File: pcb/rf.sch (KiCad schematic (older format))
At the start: 28 parts, among them U3 STM32W108C8, U4 SE2432L

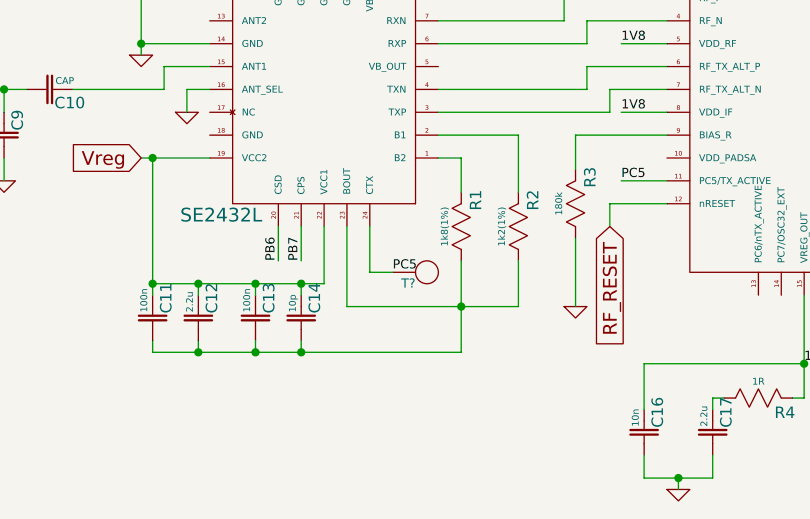
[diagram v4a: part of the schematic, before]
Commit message: Added MCP6409 and audio preamp schematic
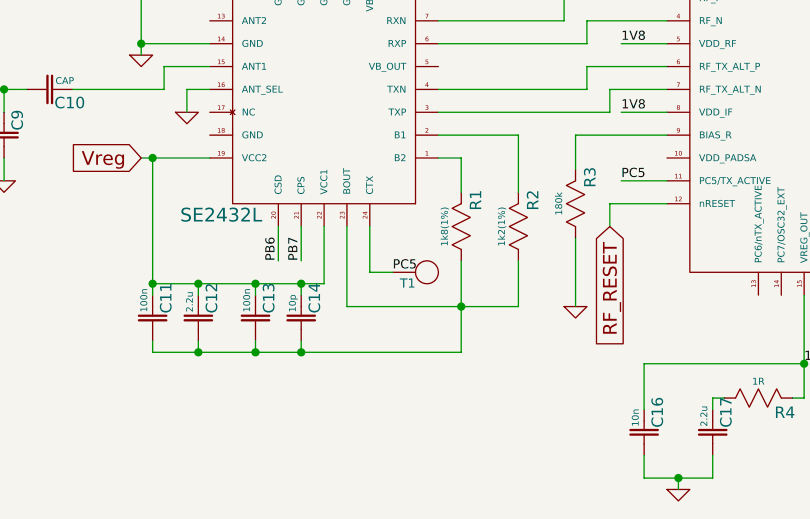
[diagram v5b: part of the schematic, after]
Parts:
- gave numbers to parts that had none: 1
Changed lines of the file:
@@
-EESchema Schematic File Version 2  date 7/25/2012 8:49:54 PM
+EESchema Schematic File Version 2  date Thu 26 Jul 2012 01:52:34 AM EDT
 LIBS:power
 LIBS:device
@@
 LIBS:valves
 LIBS:f4_daughter
+LIBS:f4_daughter-cache
 EELAYER 25  0
 EELAYER END
-$Descr A4 11700 8267
+$Descr A4 11693 8268
 encoding utf-8
-Sheet 2 4
+Sheet 2 5
 Title ""
 Date "26 jul 2012"
@@
 PC5
 $Comp
-L GND #PWR01
+L GND #PWR13
 U 1 1 500DD937
 P 8250 4650
-F 0 "#PWR01" H 8250 4650 30  0001 C CNN
+F 0 "#PWR13" H 8250 4650 30  0001 C CNN
 F 1 "GND" H 8250 4580 30  0001 C CNN
 	1    8250 4650
@@
 $EndComp
 $Comp
-L GND #PWR02
+L GND #PWR5
 U 1 1 500DD8E1
 P 3850 4200
-F 0 "#PWR02" H 3850 4200 30  0001 C CNN
+F 0 "#PWR5" H 3850 4200 30  0001 C CNN
 F 1 "GND" H 3850 4130 30  0001 C CNN
 	1    3850 4200
@@
 $EndComp
 $Comp
-L GND #PWR03
+L GND #PWR12
 U 1 1 500DD883
 P 8100 3050
-F 0 "#PWR03" H 8100 3050 30  0001 C CNN
+F 0 "#PWR12" H 8100 3050 30  0001 C CNN
 F 1 "GND" H 8100 2980 30  0001 C CNN
 	1    8100 3050
@@
 1V2
 $Comp
-L GND #PWR04
+L GND #PWR8
 U 1 1 500DD7C0
 P 5800 3200
-F 0 "#PWR04" H 5800 3200 30  0001 C CNN
+F 0 "#PWR8" H 5800 3200 30  0001 C CNN
 F 1 "GND" H 5800 3130 30  0001 C CNN
 	1    5800 3200
@@
 $EndComp
 $Comp
-L GND #PWR05
+L GND #PWR10
 U 1 1 500DD6F0
 P 7550 5650
-F 0 "#PWR05" H 7550 5650 30  0001 C CNN
+F 0 "#PWR10" H 7550 5650 30  0001 C CNN
 F 1 "GND" H 7550 5580 30  0001 C CNN
 	1    7550 5650
@@
 Vreg
 $Comp
-L GND #PWR06
+L GND #PWR6
 U 1 1 500DD2FF
 P 5000 3650
-F 0 "#PWR06" H 5000 3650 30  0001 C CNN
+F 0 "#PWR6" H 5000 3650 30  0001 C CNN
 F 1 "GND" H 5000 3580 30  0001 C CNN
 	1    5000 3650
@@
 $EndComp
 $Comp
-L GND #PWR07
+L GND #PWR9
 U 1 1 500DD1EA
 P 6000 5850
-F 0 "#PWR07" H 6000 5850 30  0001 C CNN
+F 0 "#PWR9" H 6000 5850 30  0001 C CNN
 F 1 "GND" H 6000 5780 30  0001 C CNN
 	1    6000 5850
@@
 $EndComp
 $Comp
-L GND #PWR08
+L GND #PWR7
 U 1 1 500DCCCC
 P 5550 5050
-F 0 "#PWR08" H 5550 5050 30  0001 C CNN
+F 0 "#PWR7" H 5550 5050 30  0001 C CNN
 F 1 "GND" H 5550 4980 30  0001 C CNN
 	1    5550 5050
@@
 1V8
 $Comp
-L GND #PWR09
+L GND #PWR3
 U 1 1 500DCAB4
 P 3050 4500
-F 0 "#PWR09" H 3050 4500 30  0001 C CNN
+F 0 "#PWR3" H 3050 4500 30  0001 C CNN
 F 1 "GND" H 3050 4430 30  0001 C CNN
 	1    3050 4500
@@
 $EndComp
 $Comp
-L GND #PWR010
+L GND #PWR2
 U 1 1 500DCAB1
 P 2200 4500
-F 0 "#PWR010" H 2200 4500 30  0001 C CNN
+F 0 "#PWR2" H 2200 4500 30  0001 C CNN
 F 1 "GND" H 2200 4430 30  0001 C CNN
 	1    2200 4500
@@
 $EndComp
 $Comp
-L GND #PWR011
+L GND #PWR4
 U 1 1 500DCAA7
 P 3650 3950
-F 0 "#PWR011" H 3650 3950 30  0001 C CNN
+F 0 "#PWR4" H 3650 3950 30  0001 C CNN
 F 1 "GND" H 3650 3880 30  0001 C CNN
 	1    3650 3950
@@
 $EndComp
 $Comp
-L GND #PWR012
+L GND #PWR1
 U 1 1 500DCA40
 P 1800 4200
-F 0 "#PWR012" H 1800 4200 30  0001 C CNN
+F 0 "#PWR1" H 1800 4200 30  0001 C CNN
 F 1 "GND" H 1800 4130 30  0001 C CNN
 	1    1800 4200
@@
 $EndComp
 $Comp
-L GND #PWR013
+L GND #PWR11
 U 1 1 500DCA3C
 P 8050 4950
-F 0 "#PWR013" H 8050 4950 30  0001 C CNN
+F 0 "#PWR11" H 8050 4950 30  0001 C CNN
 F 1 "GND" H 8050 4880 30  0001 C CNN
 	1    8050 4950
@@
 $EndComp
 $Comp
-L TP T?
+L TP T1
 U 1 1 500EC307
 P 4850 4900
-F 0 "T?" H 4850 4875 40  0000 R TNN
+F 0 "T1" H 4850 4875 40  0000 R TNN
 F 1 "TP" H 4800 4950 60  0001 C CNN
 	1    4850 4900

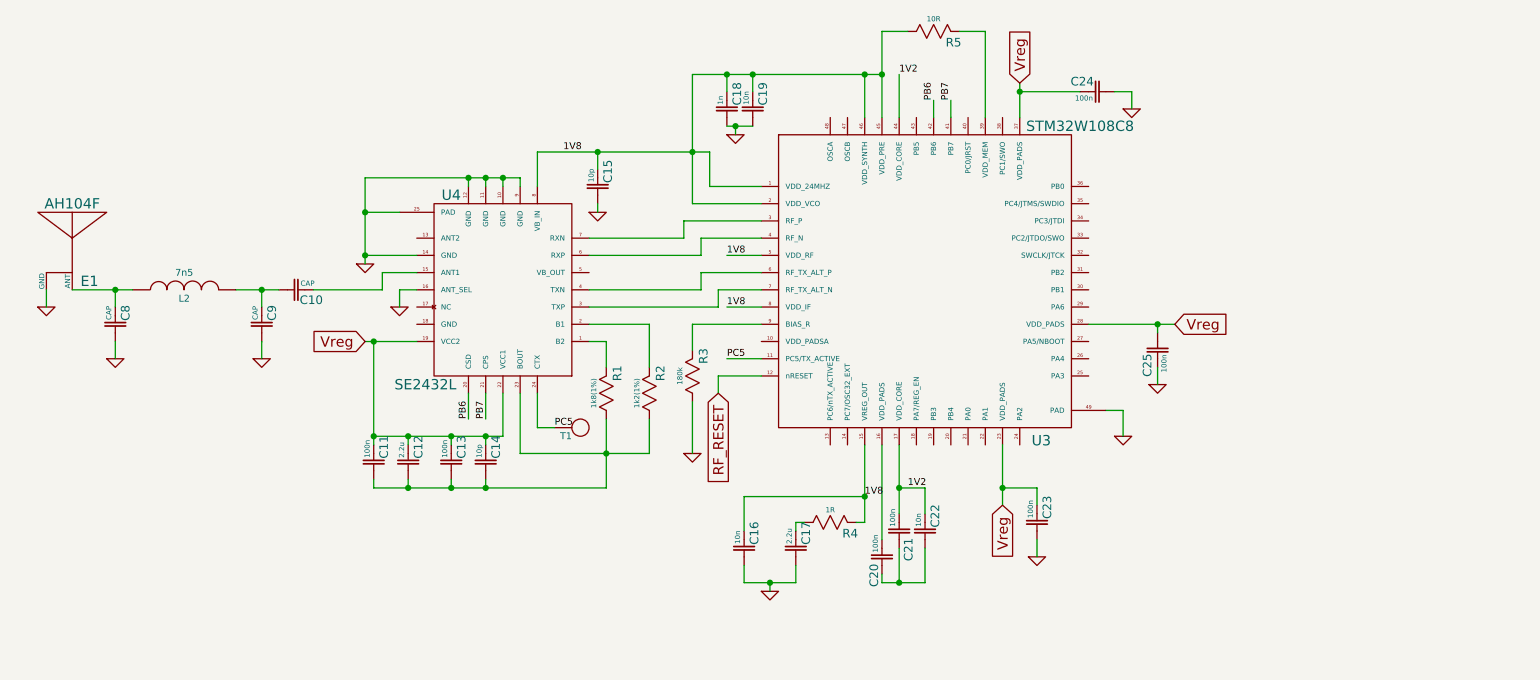
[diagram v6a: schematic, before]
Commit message: Added LCD and started wiring busses
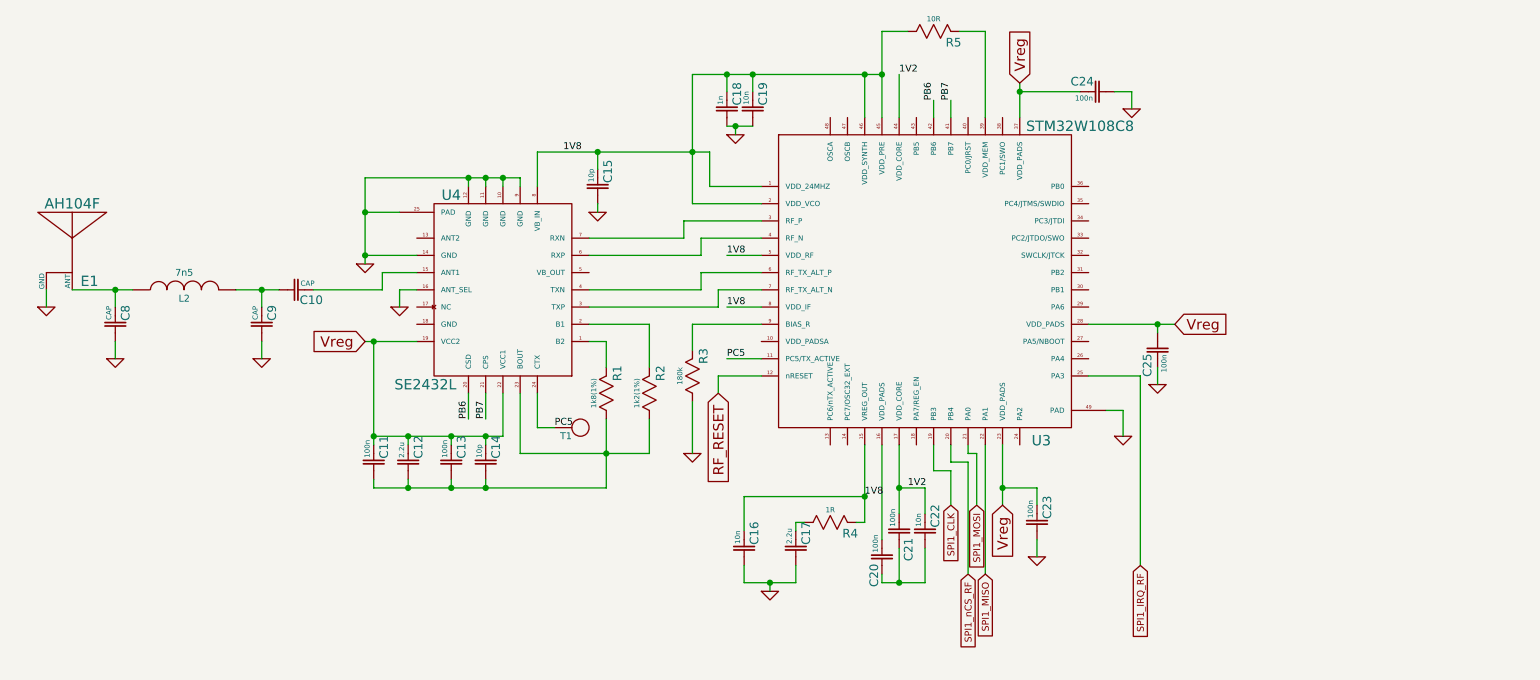
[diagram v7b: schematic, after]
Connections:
- net SPI1_CLK: now reaches U3.19 (PB3)
- net SPI1_nCS_RF: now reaches U3.20 (PB4)
- net SPI1_MOSI: now reaches U3.21 (PA0)
- net SPI1_MISO: now reaches U3.22 (PA1)
- net SPI1_IRQ_RF: now reaches U3.25 (PA3)
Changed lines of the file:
@@
-EESchema Schematic File Version 2  date Thu 26 Jul 2012 02:06:26 AM EDT
+EESchema Schematic File Version 2  date Thu 26 Jul 2012 11:54:13 PM EDT
 LIBS:power
 LIBS:device
@@
 Sheet 2 5
 Title ""
-Date "26 jul 2012"
+Date "27 jul 2012"
 Rev ""
 Comp ""
@@
 Connection ~ 6650 2850
 Wire Wire Line
-	6650 3100 6650 2600
+	6650 2600 6650 3100
 Wire Wire Line
 	6650 2600 6800 2600
@@
 Connection ~ 5550 3300
 Wire Wire Line
-	5650 3300 4650 3300
+	4650 3300 5650 3300
 Wire Wire Line
 	5650 3300 5650 3500
@@
 Connection ~ 3700 4950
 Wire Wire Line
-	3700 5000 3700 4400
+	3700 4400 3700 5000
 Wire Wire Line
 	3650 4400 3950 4400
@@
 Connection ~ 5050 5050
 Wire Wire Line
-	5300 5050 4550 5050
+	4550 5050 5300 5050
 Wire Wire Line
 	4950 4300 5300 4300
@@
 	3650 3450 4550 3450
 Wire Wire Line
-	3650 3950 3650 3450
+	3650 3450 3650 3950
 Connection ~ 3650 3650
 Connection ~ 4250 3450
@@
 	6150 5800 6150 5700
 Wire Wire Line
-	6150 5800 5850 5800
+	5850 5800 6150 5800
 Wire Wire Line
 	5850 5800 5850 5700
@@
 	5550 2850 5550 3600
 Wire Wire Line
-	6650 2850 5550 2850
+	5550 2850 6650 2850
 Wire Wire Line
 	6750 3100 6750 2850
@@
 	1    0    0    -1
 $EndComp
+Text GLabel 7050 5350 3    40   Input ~ 0
+SPI1_CLK
+Wire Wire Line
+	7050 5350 7050 5150
+Wire Wire Line
+	7050 5150 6950 5150
+Wire Wire Line
+	6950 5150 6950 5000
+Text GLabel 7150 5750 3    40   Input ~ 0
+SPI1_nCS_RF
+Wire Wire Line
+	7150 5750 7150 5100
+Wire Wire Line
+	7150 5100 7050 5100
+Wire Wire Line
+	7050 5100 7050 5000
+Text GLabel 7200 5350 3    40   Input ~ 0
+SPI1_MOSI
+Wire Wire Line
+	7200 5350 7200 5050
+Wire Wire Line
+	7200 5050 7150 5050
+Wire Wire Line
+	7150 5050 7150 5000
+Text GLabel 7250 5750 3    40   Input ~ 0
+SPI1_MISO
+Wire Wire Line
+	7250 5750 7250 5000
+Text GLabel 8150 5700 3    40   Input ~ 0
+SPI1_IRQ_RF
+Wire Wire Line
+	8150 5700 8150 4600
+Wire Wire Line
+	8150 4600 7850 4600
 $EndSCHEMATC

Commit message: Broke up schematic in a more modular fashion -- Added LCD footprint
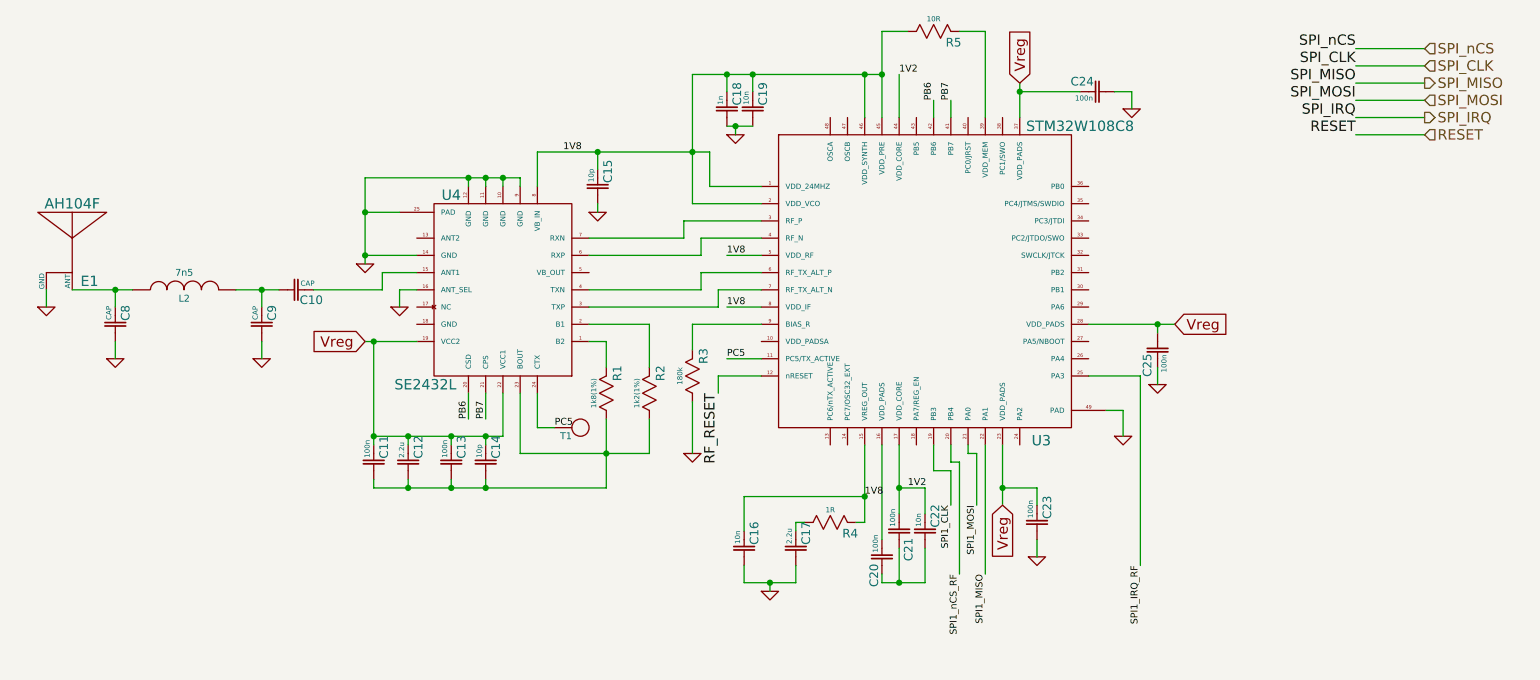
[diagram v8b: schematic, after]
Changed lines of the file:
@@
-EESchema Schematic File Version 2  date Thu 26 Jul 2012 11:54:13 PM EDT
+EESchema Schematic File Version 2  date Tue 31 Jul 2012 10:29:35 PM EDT
 LIBS:power
 LIBS:device
@@
 EELAYER 25  0
 EELAYER END
-$Descr A4 11693 8268
+$Descr A4 11700 8267
 encoding utf-8
-Sheet 2 5
+Sheet 4 6
 Title ""
-Date "27 jul 2012"
+Date "1 aug 2012"
 Rev ""
 Comp ""
@@
 $EndDescr
 Wire Wire Line
+	9800 2700 9400 2700
+Wire Wire Line
+	9800 2900 9400 2900
+Wire Wire Line
+	9800 3100 9400 3100
+Wire Wire Line
 	7050 3000 7050 3100
 Wire Wire Line
@@
 Connection ~ 8250 4300
 Wire Wire Line
-	7850 4300 8350 4300
+	8350 4300 7850 4300
 Connection ~ 6650 2850
 Wire Wire Line
-	6650 2600 6650 3100
+	6650 3100 6650 2600
 Wire Wire Line
 	6650 2600 6800 2600
@@
 Connection ~ 5800 3150
 Wire Wire Line
-	5750 3150 5900 3150
+	5900 3150 5750 3150
 Connection ~ 5550 3300
 Wire Wire Line
-	4650 3300 5650 3300
+	5650 3300 4650 3300
 Wire Wire Line
 	5650 3300 5650 3500
@@
 	5650 3500 5950 3500
 Wire Wire Line
-	6650 5800 6650 5750
+	6650 5750 6650 5800
 Wire Wire Line
 	6750 5600 6750 5800
@@
 Connection ~ 6750 5250
 Wire Wire Line
-	6900 5250 6750 5250
+	6750 5250 6900 5250
 Wire Wire Line
 	6900 5250 6900 5400
 Connection ~ 7350 5250
 Wire Wire Line
-	7550 5250 7350 5250
+	7350 5250 7550 5250
 Wire Wire Line
 	7550 5250 7550 5350
@@
 	3900 5250 3900 5200
 Wire Wire Line
-	3700 5250 3700 5200
+	3700 5200 3700 5250
 Connection ~ 4150 4950
 Wire Wire Line
@@
 Connection ~ 3700 4950
 Wire Wire Line
-	3700 4400 3700 5000
-Wire Wire Line
-	3650 4400 3950 4400
+	3700 5000 3700 4400
+Wire Wire Line
+	3950 4400 3650 4400
 Connection ~ 6550 5300
 Wire Wire Line
-	5850 5300 6550 5300
+	6550 5300 5850 5300
 Wire Wire Line
 	5850 5300 5850 5500
@@
 	5000 3650 5000 3600
 Wire Wire Line
-	6550 5450 6500 5450
-Wire Wire Line
-	6550 5000 6550 5450
-Wire Wire Line
-	5300 5050 5300 4850
+	6500 5450 6550 5450
+Wire Wire Line
+	6550 5450 6550 5000
+Wire Wire Line
+	5300 4850 5300 5050
 Wire Wire Line
 	5050 4550 5050 4400
 Connection ~ 5050 5050
 Wire Wire Line
-	4550 5050 5300 5050
+	5300 5050 4550 5050
 Wire Wire Line
 	4950 4300 5300 4300
@@
 Connection ~ 4450 3450
 Wire Wire Line
-	4550 3450 4550 3500
+	4550 3500 4550 3450
 Wire Wire Line
 	4350 3450 4350 3500
@@
 Connection ~ 2200 4100
 Wire Wire Line
-	1950 4100 2300 4100
+	2300 4100 1950 4100
 Wire Wire Line
 	1800 4200 1800 4100
 Wire Wire Line
-	2900 4100 3150 4100
+	3150 4100 2900 4100
 Connection ~ 3050 4100
 Wire Wire Line
@@
 Connection ~ 4350 3450
 Wire Wire Line
-	3650 3450 4550 3450
+	4550 3450 3650 3450
 Wire Wire Line
 	3650 3450 3650 3950
@@
 	3750 4100 3350 4100
 Wire Wire Line
-	6150 5800 6150 5700
-Wire Wire Line
-	5850 5800 6150 5800
+	6150 5700 6150 5800
+Wire Wire Line
+	6150 5800 5850 5800
 Wire Wire Line
 	5850 5800 5850 5700
@@
 Connection ~ 3900 5250
 Wire Wire Line
-	5050 5250 3700 5250
-Wire Wire Line
-	5050 4850 5050 5250
+	3700 5250 5050 5250
+Wire Wire Line
+	5050 5250 5050 4850
 Connection ~ 4350 5250
 Wire Wire Line
-	7350 5000 7350 5350
+	7350 5350 7350 5000
 Wire Wire Line
 	7550 5650 7550 5550
 Wire Wire Line
-	6750 5000 6750 5400
+	6750 5400 6750 5000
 Wire Wire Line
 	6650 5800 6900 5800
@@
 	6900 5800 6900 5600
 Wire Wire Line
-	5550 3600 5950 3600
+	5950 3600 5550 3600
 Connection ~ 5000 3300
 Wire Wire Line
 	5800 3200 5800 3150
 Wire Wire Line
-	5550 2850 5550 3600
+	5550 3600 5550 2850
 Wire Wire Line
 	5550 2850 6650 2850
@@
 	8100 2950 8000 2950
 Wire Wire Line
-	7450 2900 7450 3100
+	7450 3100 7450 2900
 Connection ~ 7450 2950
 Wire Wire Line
@@
 Wire Wire Line
 	6950 3000 6950 3100
+Wire Wire Line
+	7050 5350 7050 5150
+Wire Wire Line
+	7050 5150 6950 5150
+Wire Wire Line
+	6950 5150 6950 5000
+Wire Wire Line
+	7100 5750 7100 5100
+Wire Wire Line
+	7100 5100 7050 5100
+Wire Wire Line
+	7050 5100 7050 5000
+Wire Wire Line
+	7200 5350 7200 5050
+Wire Wire Line
+	7200 5050 7150 5050
+Wire Wire Line
+	7150 5050 7150 5000
+Wire Wire Line
+	7250 5750 7250 5000
+Wire Wire Line
+	8150 5700 8150 4600
+Wire Wire Line
+	8150 4600 7850 4600
+Wire Wire Line
+	9800 3200 9400 3200
+Wire Wire Line
+	9400 3000 9800 3000
+Wire Wire Line
+	9400 2800 9800 2800
+Text HLabel 9800 3200 2    60   Input ~ 0
+RESET
+Text Label 9400 3100 2    60   ~ 0
+SPI_IRQ
+Text Label 9400 3000 2    60   ~ 0
+SPI_MOSI
+Text Label 9400 2900 2    60   ~ 0
+SPI_MISO
+Text Label 9400 2800 2    60   ~ 0
+SPI_CLK
+Text Label 9400 2700 2    60   ~ 0
+SPI_nCS
+Text Label 9400 3200 2    60   ~ 0
+RESET
+Text Label 5700 4700 3    60   ~ 0
+RF_RESET
+Text Label 8150 5700 3    40   ~ 0
+SPI1_IRQ_RF
+Text Label 7250 5750 3    40   ~ 0
+SPI1_MISO
+Text Label 7200 5350 3    40   ~ 0
+SPI1_MOSI
+Text Label 7100 5750 3    40   ~ 0
+SPI1_nCS_RF
+Text Label 7050 5350 3    40   ~ 0
+SPI1_CLK
+Text HLabel 9800 3100 2    60   Output ~ 0
+SPI_IRQ
+Text HLabel 9800 3000 2    60   Input ~ 0
+SPI_MOSI
+Text HLabel 9800 2900 2    60   Output ~ 0
+SPI_MISO
+Text HLabel 9800 2800 2    60   Input ~ 0
+SPI_CLK
+Text HLabel 9800 2700 2    60   Input ~ 0
+SPI_nCS
 Text Label 6950 3000 1    40   ~ 0
 PB6
@@
 Text Label 4250 4850 1    40   ~ 0
 PB6
-Text GLabel 5700 4700 3    60   Input ~ 0
-RF_RESET
 Text Label 5750 4500 0    40   ~ 0
 PC5
@@
 PC5
 $Comp
-L GND #PWR13
+L GND #PWR07
 U 1 1 500DD937
 P 8250 4650
-F 0 "#PWR13" H 8250 4650 30  0001 C CNN
+F 0 "#PWR07" H 8250 4650 30  0001 C CNN
 F 1 "GND" H 8250 4580 30  0001 C CNN
 	1    8250 4650
@@
 $EndComp
 $Comp
-L GND #PWR5
+L GND #PWR08
 U 1 1 500DD8E1
 P 3850 4200
-F 0 "#PWR5" H 3850 4200 30  0001 C CNN
+F 0 "#PWR08" H 3850 4200 30  0001 C CNN
 F 1 "GND" H 3850 4130 30  0001 C CNN
 	1    3850 4200
@@
 $EndComp
 $Comp
-L GND #PWR12
+L GND #PWR09
 U 1 1 500DD883
 P 8100 3050
-F 0 "#PWR12" H 8100 3050 30  0001 C CNN
+F 0 "#PWR09" H 8100 3050 30  0001 C CNN
 F 1 "GND" H 8100 2980 30  0001 C CNN
 	1    8100 3050
@@
 1V2
 $Comp
-L GND #PWR8
+L GND #PWR010
 U 1 1 500DD7C0
 P 5800 3200
-F 0 "#PWR8" H 5800 3200 30  0001 C CNN
+F 0 "#PWR010" H 5800 3200 30  0001 C CNN
 F 1 "GND" H 5800 3130 30  0001 C CNN
 	1    5800 3200
@@
 $EndComp
 $Comp
-L GND #PWR10
+L GND #PWR011
 U 1 1 500DD6F0
 P 7550 5650
-F 0 "#PWR10" H 7550 5650 30  0001 C CNN
+F 0 "#PWR011" H 7550 5650 30  0001 C CNN
 F 1 "GND" H 7550 5580 30  0001 C CNN
 	1    7550 5650
@@
 Vreg
 $Comp
-L GND #PWR6
+L GND #PWR012
 U 1 1 500DD2FF
 P 5000 3650
-F 0 "#PWR6" H 5000 3650 30  0001 C CNN
+F 0 "#PWR012" H 5000 3650 30  0001 C CNN
 F 1 "GND" H 5000 3580 30  0001 C CNN
 	1    5000 3650
@@
 $EndComp
 $Comp
-L GND #PWR9
+L GND #PWR013
 U 1 1 500DD1EA
 P 6000 5850
-F 0 "#PWR9" H 6000 5850 30  0001 C CNN
+F 0 "#PWR013" H 6000 5850 30  0001 C CNN
 F 1 "GND" H 6000 5780 30  0001 C CNN
 	1    6000 5850
@@
 $EndComp
 $Comp
-L GND #PWR7
+L GND #PWR014
 U 1 1 500DCCCC
 P 5550 5050
-F 0 "#PWR7" H 5550 5050 30  0001 C CNN
+F 0 "#PWR014" H 5550 5050 30  0001 C CNN
 F 1 "GND" H 5550 4980 30  0001 C CNN
 	1    5550 5050
@@
 1V8
 $Comp
-L GND #PWR3
+L GND #PWR015
 U 1 1 500DCAB4
 P 3050 4500
-F 0 "#PWR3" H 3050 4500 30  0001 C CNN
+F 0 "#PWR015" H 3050 4500 30  0001 C CNN
 F 1 "GND" H 3050 4430 30  0001 C CNN
 	1    3050 4500
@@
 $EndComp
 $Comp
-L GND #PWR2
+L GND #PWR016
 U 1 1 500DCAB1
 P 2200 4500
-F 0 "#PWR2" H 2200 4500 30  0001 C CNN
+F 0 "#PWR016" H 2200 4500 30  0001 C CNN
 F 1 "GND" H 2200 4430 30  0001 C CNN
 	1    2200 4500
@@
 $EndComp
 $Comp
-L GND #PWR4
+L GND #PWR017
 U 1 1 500DCAA7
 P 3650 3950
-F 0 "#PWR4" H 3650 3950 30  0001 C CNN
+F 0 "#PWR017" H 3650 3950 30  0001 C CNN
 F 1 "GND" H 3650 3880 30  0001 C CNN
 	1    3650 3950
@@
 $EndComp
 $Comp
-L GND #PWR1
+L GND #PWR018
 U 1 1 500DCA40
 P 1800 4200
-F 0 "#PWR1" H 1800 4200 30  0001 C CNN
+F 0 "#PWR018" H 1800 4200 30  0001 C CNN
 F 1 "GND" H 1800 4130 30  0001 C CNN
 	1    1800 4200
@@
 $EndComp
 $Comp
-L GND #PWR11
+L GND #PWR019
 U 1 1 500DCA3C
 P 8050 4950
-F 0 "#PWR11" H 8050 4950 30  0001 C CNN
+F 0 "#PWR019" H 8050 4950 30  0001 C CNN
 F 1 "GND" H 8050 4880 30  0001 C CNN
 	1    8050 4950
@@
 	1    0    0    -1
 $EndComp
-Text GLabel 7050 5350 3    40   Input ~ 0
-SPI1_CLK
-Wire Wire Line
-	7050 5350 7050 5150
-Wire Wire Line
-	7050 5150 6950 5150
-Wire Wire Line
-	6950 5150 6950 5000
-Text GLabel 7150 5750 3    40   Input ~ 0
-SPI1_nCS_RF
-Wire Wire Line
-	7150 5750 7150 5100
-Wire Wire Line
-	7150 5100 7050 5100
-Wire Wire Line
-	7050 5100 7050 5000
-Text GLabel 7200 5350 3    40   Input ~ 0
-SPI1_MOSI
-Wire Wire Line
-	7200 5350 7200 5050
-Wire Wire Line
-	7200 5050 7150 5050
-Wire Wire Line
-	7150 5050 7150 5000
-Text GLabel 7250 5750 3    40   Input ~ 0
-SPI1_MISO
-Wire Wire Line
-	7250 5750 7250 5000
-Text GLabel 8150 5700 3    40   Input ~ 0
-SPI1_IRQ_RF
-Wire Wire Line
-	8150 5700 8150 4600
-Wire Wire Line
-	8150 4600 7850 4600
 $EndSCHEMATC
